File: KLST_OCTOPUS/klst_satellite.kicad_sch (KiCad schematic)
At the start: 2 parts

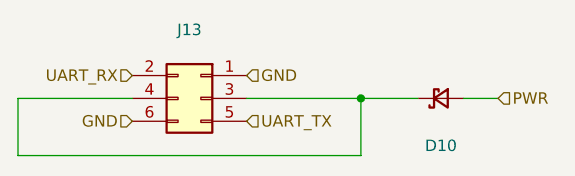
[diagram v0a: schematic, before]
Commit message: renamed project, routed traces
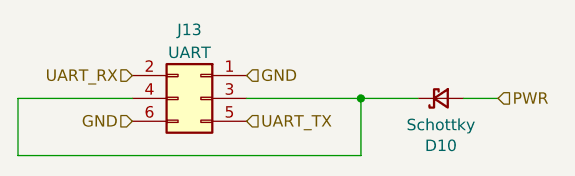
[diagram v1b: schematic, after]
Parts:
- D10: value (none) -> Schottky; footprint (none) -> Diode_SMD:D_SOD-123
- J13: value (none) -> UART; footprint (none) -> Connector_IDC:IDC-Header_2x03_P2.54mm_Horizontal
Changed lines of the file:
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@@
     (in_bom yes) (on_board yes)
     (property "Reference" "J13" (id 0) (at 142.24 88.9 0))
-    (property "Value" "" (id 1) (at 142.24 91.44 0))
-    (property "Footprint" "" (id 2) (at 143.51 96.52 0)
+    (property "Value" "UART" (id 1) (at 142.24 91.44 0))
+    (property "Footprint" "Connector_IDC:IDC-Header_2x03_P2.54mm_Horizontal" (id 2) (at 143.51 96.52 0)
       (effects (font (size 1.27 1.27)) hide)
     )
@@
     (in_bom yes) (on_board yes)
     (property "Reference" "D10" (id 0) (at 170.18 101.7778 0))
-    (property "Value" "" (id 1) (at 170.18 99.4664 0))
-    (property "Footprint" "" (id 2) (at 170.18 96.52 90)
+    (property "Value" "Schottky" (id 1) (at 170.18 99.4664 0))
+    (property "Footprint" "Diode_SMD:D_SOD-123" (id 2) (at 170.18 96.52 90)
       (effects (font (size 1.27 1.27)) hide)
     )

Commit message: finalized PCB
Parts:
- D10: MFR.Part # B5819W -> B5819W SL; MPN SS1040_R1_00001 -> (none)
- J13: footprint Connector_IDC:IDC-Header_2x03_P2.54mm_Horizontal -> (none); MFR.Part # 300R-6P -> B-3000R06P-0110
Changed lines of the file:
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@@
     (property "Reference" "J13" (id 0) (at 142.24 88.9 0))
     (property "Value" "UART" (id 1) (at 142.24 91.44 0))
-    (property "Footprint" "Connector_IDC:IDC-Header_2x03_P2.54mm_Horizontal" (id 2) (at 143.51 96.52 0)
+    (property "Footprint" "" (id 2) (at 143.51 96.52 0)
       (effects (font (size 1.27 1.27)) hide)
     )
@@
       (effects (font (size 1.27 1.27)) hide)
     )
-    (property "MFR.Part #" "300R-6P" (id 4) (at 143.51 96.52 0)
+    (property "MFR.Part #" "B-3000R06P-0110" (id 4) (at 143.51 96.52 0)
       (effects (font (size 1.27 1.27)) hide)
     )
@@
       (effects (font (size 1.27 1.27)) hide)
     )
-    (property "MFR.Part #" "B5819W" (id 4) (at 170.18 96.52 0)
+    (property "MFR.Part #" "B5819W SL" (id 4) (at 170.18 96.52 0)
       (effects (font (size 1.27 1.27)) hide)
     )
@@
       (effects (font (size 1.27 1.27)) hide)
     )
-    (property "MPN" "SS1040_R1_00001" (id 8) (at 170.18 96.52 0)
+    (property "MPN" "" (id 8) (at 170.18 96.52 0)
       (effects (font (size 1.27 1.27)) hide)
     )

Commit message: fixed schematics
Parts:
- J13: footprint (none) -> Connector_IDC:IDC-Header_2x03_P2.54mm_Horizontal
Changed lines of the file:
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@@
     (property "Reference" "J13" (id 0) (at 142.24 88.9 0))
     (property "Value" "UART" (id 1) (at 142.24 91.44 0))
-    (property "Footprint" "" (id 2) (at 143.51 96.52 0)
+    (property "Footprint" "Connector_IDC:IDC-Header_2x03_P2.54mm_Horizontal" (id 2) (at 143.51 96.52 0)
       (effects (font (size 1.27 1.27)) hide)
     )

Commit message: updated LCSC #
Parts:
- D10: LCSC Part # (none) -> C8598
- J13: LCSC Part # (none) -> C146629
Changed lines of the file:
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@@
       (effects (font (size 1.27 1.27)) hide)
     )
-    (property "LCSC Part #" "" (id 5) (at 143.51 96.52 0)
+    (property "LCSC Part #" "C146629" (id 5) (at 143.51 96.52 0)
       (effects (font (size 1.27 1.27)) hide)
     )
@@
       (effects (font (size 1.27 1.27)) hide)
     )
-    (property "LCSC Part #" "" (id 5) (at 170.18 96.52 0)
+    (property "LCSC Part #" "C8598" (id 5) (at 170.18 96.52 0)
       (effects (font (size 1.27 1.27)) hide)
     )

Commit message: prepared components for production
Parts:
- D10: JLCPCB Part # C8598 -> (none); LCSC (none) -> C8598; LCSC Part # C8598 -> (none); MFR.Part # B5819W SL -> (none)
- J13: JLCPCB Part # C146629 -> (none); LCSC (none) -> C146629; LCSC Part # C146629 -> (none); MFR.Part # B-3000R06P-0110 -> (none)
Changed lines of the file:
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@@
       (effects (font (size 1.27 1.27)) hide)
     )
-    (property "MFR.Part #" "B-3000R06P-0110" (id 4) (at 143.51 96.52 0)
-      (effects (font (size 1.27 1.27)) hide)
-    )
-    (property "LCSC Part #" "C146629" (id 5) (at 143.51 96.52 0)
+    (property "LCSC" "C146629" (id 5) (at 143.51 96.52 0)
       (effects (font (size 1.27 1.27)) hide)
     )
     (property "Extended Part" "-" (id 6) (at 143.51 96.52 0)
-      (effects (font (size 1.27 1.27)) hide)
-    )
-    (property "JLCPCB Part #" "C146629" (id 7) (at 143.51 96.52 0)
       (effects (font (size 1.27 1.27)) hide)
     )
@@
       (effects (font (size 1.27 1.27)) hide)
     )
-    (property "MFR.Part #" "B5819W SL" (id 4) (at 170.18 96.52 0)
-      (effects (font (size 1.27 1.27)) hide)
-    )
-    (property "LCSC Part #" "C8598" (id 5) (at 170.18 96.52 0)
+    (property "LCSC" "C8598" (id 5) (at 170.18 96.52 0)
       (effects (font (size 1.27 1.27)) hide)
     )
@@
       (effects (font (size 1.27 1.27)) hide)
     )
-    (property "JLCPCB Part #" "C8598" (id 7) (at 170.18 96.52 0)
-      (effects (font (size 1.27 1.27)) hide)
-    )
-    (property "MPN" "" (id 8) (at 170.18 96.52 0)
-      (effects (font (size 1.27 1.27)) hide)
-    )

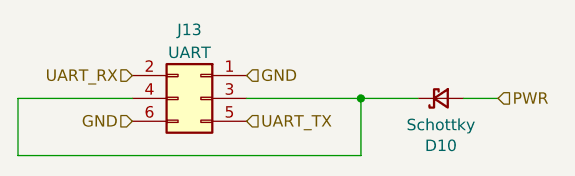
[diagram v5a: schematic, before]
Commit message: fixed bug with TX + buffer
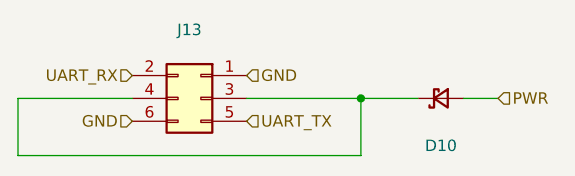
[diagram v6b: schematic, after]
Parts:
- D10: value Schottky -> (none); footprint Diode_SMD:D_SOD-123 -> (none)
- J13: value UART -> (none); footprint Connector_IDC:IDC-Header_2x03_P2.54mm_Horizontal -> (none)
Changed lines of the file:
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@@
     (in_bom yes) (on_board yes)
     (property "Reference" "J13" (id 0) (at 142.24 88.9 0))
-    (property "Value" "UART" (id 1) (at 142.24 91.44 0))
-    (property "Footprint" "Connector_IDC:IDC-Header_2x03_P2.54mm_Horizontal" (id 2) (at 143.51 96.52 0)
+    (property "Value" "" (id 1) (at 142.24 91.44 0))
+    (property "Footprint" "" (id 2) (at 143.51 96.52 0)
       (effects (font (size 1.27 1.27)) hide)
     )
@@
     (in_bom yes) (on_board yes)
     (property "Reference" "D10" (id 0) (at 170.18 101.7778 0))
-    (property "Value" "Schottky" (id 1) (at 170.18 99.4664 0))
-    (property "Footprint" "Diode_SMD:D_SOD-123" (id 2) (at 170.18 96.52 90)
+    (property "Value" "" (id 1) (at 170.18 99.4664 0))
+    (property "Footprint" "" (id 2) (at 170.18 96.52 90)
       (effects (font (size 1.27 1.27)) hide)
     )
